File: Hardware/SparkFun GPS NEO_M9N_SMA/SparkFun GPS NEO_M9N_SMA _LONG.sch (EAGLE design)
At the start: 51 parts, among them J2 Qwiic Right Angle, J4 Qwiic Right Angle, U1 U-BLOX_NEO-M9N, U2 3.3V

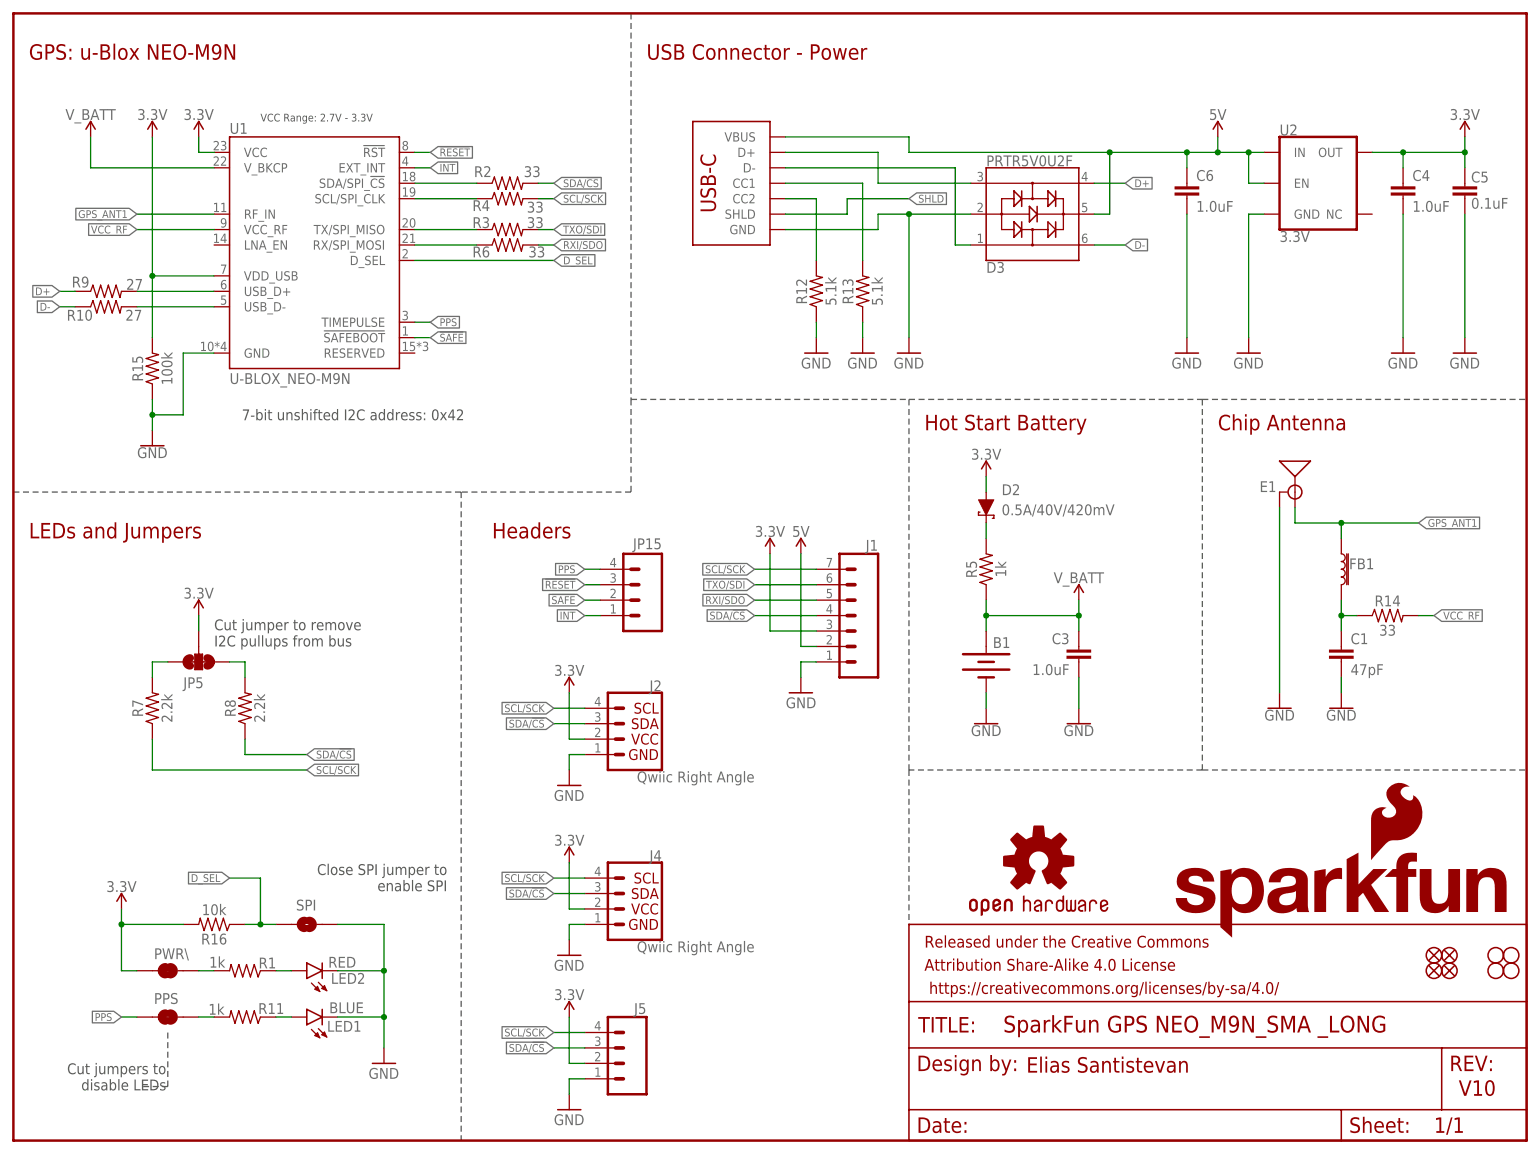
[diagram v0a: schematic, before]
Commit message: Updates SMD, SMA connector with new footprint
* Fixes connector label in schematic
* Fixes LED labels
* Fixes TX/SDO label
* Adds VCC Range to regulator
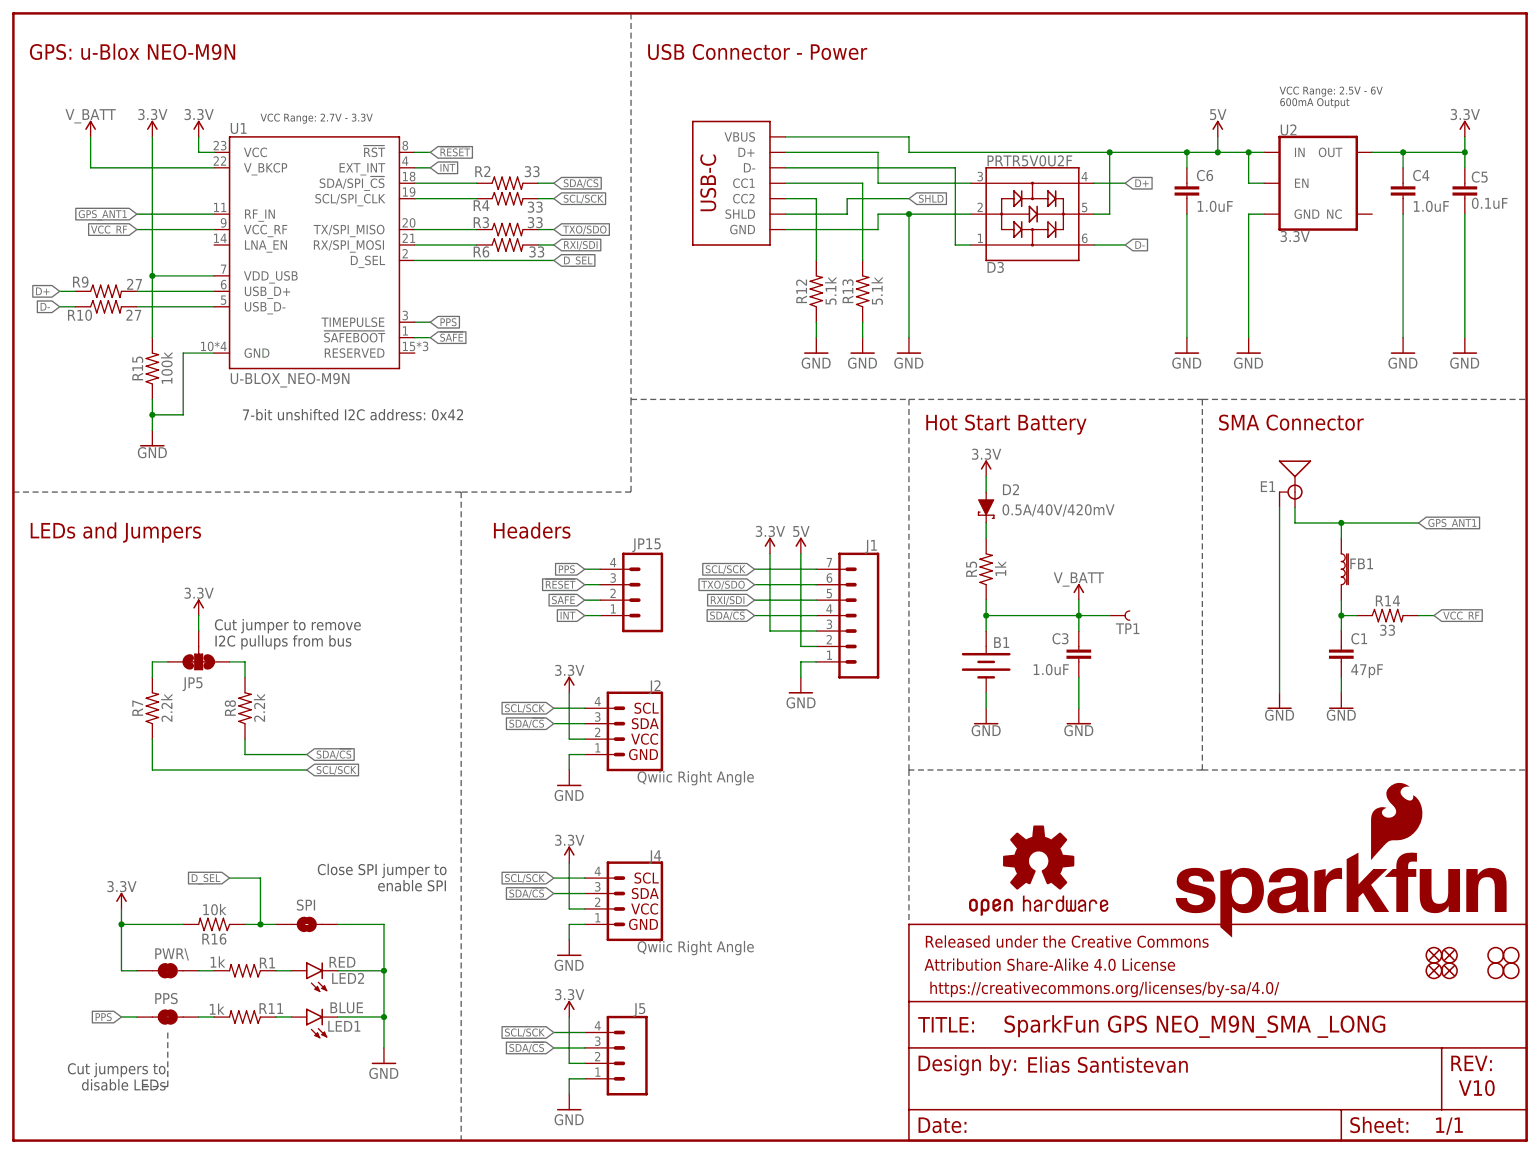
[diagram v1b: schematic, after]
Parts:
- added TP1: TEST-POINT3X4, SparkFun-Connectors:TEST-POINT3X4
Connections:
- net RXI/SDO renamed RXI/SDI
- net TXO/SDI renamed TXO/SDO
- net V_BATT: now also TP1.1
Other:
- note added: "SMA Connector"
- note added: "VCC Range: 2.5V - 6V 600mA Output"
- note removed: "Chip Antenna"
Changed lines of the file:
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@@
 <part name="SUPPLY13" library="SparkFun-PowerSymbols" deviceset="V_BATT" device=""/>
 <part name="SUPPLY14" library="SparkFun-PowerSymbols" deviceset="V_BATT" device=""/>
+<part name="TP1" library="SparkFun-Connectors" deviceset="TEST-POINT" device="3X4"/>
 </parts>
 <sheets>
@@
 <text x="2.54" y="177.8" size="2.54" layer="94" font="vector">GPS: u-Blox NEO-M9N </text>
 <wire x1="73.66" y1="106.68" x2="73.66" y2="0" width="0.1524" layer="97" style="shortdash"/>
-<text x="198.12" y="116.84" size="2.54" layer="94" font="vector">Chip Antenna</text>
+<text x="198.12" y="116.84" size="2.54" layer="94" font="vector">SMA Connector</text>
 <wire x1="101.6" y1="121.92" x2="147.32" y2="121.92" width="0.1524" layer="97" style="shortdash"/>
 <wire x1="147.32" y1="121.92" x2="195.58" y2="121.92" width="0.1524" layer="97" style="shortdash"/>
@@
 <wire x1="21.336" y1="8.89" x2="25.4" y2="8.89" width="0.2032" layer="97" style="dashdot"/>
 <wire x1="25.4" y1="8.89" x2="25.4" y2="17.78" width="0.2032" layer="97" style="dashdot"/>
+<text x="208.28" y="170.18" size="1.27" layer="97" font="vector">VCC Range: 2.5V - 6V
+600mA Output</text>
 </plain>
 <instances>
@@
 <instance part="SUPPLY14" gate="G$1" x="12.7" y="165.1" smashed="yes">
 <attribute name="VALUE" x="12.7" y="167.894" size="1.778" layer="96" align="bottom-center"/>
+</instance>
+<instance part="TP1" gate="G$1" x="180.34" y="86.36" smashed="yes">
+<attribute name="NAME" x="181.356" y="83.312" size="1.778" layer="95" font="vector"/>
 </instance>
 </instances>
@@
 </segment>
 </net>
-<net name="RXI/SDO" class="0">
+<net name="RXI/SDI" class="0">
 <segment>
 <pinref part="R6" gate="G$1" pin="2"/>
@@
 </segment>
 </net>
-<net name="TXO/SDI" class="0">
+<net name="TXO/SDO" class="0">
 <segment>
 <pinref part="R3" gate="G$1" pin="2"/>
@@
 <pinref part="SUPPLY13" gate="G$1" pin="V_BATT"/>
 <wire x1="175.26" y1="86.36" x2="175.26" y2="88.9" width="0.1524" layer="91"/>
-</segment>
-</net>
+<pinref part="TP1" gate="G$1" pin="1"/>
+<wire x1="175.26" y1="86.36" x2="180.34" y2="86.36" width="0.1524" layer="91"/>
+</segment>
+</net>
